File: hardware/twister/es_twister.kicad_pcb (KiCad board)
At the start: 2 copper layers, 22.9 x 38.1 mm, 4 parts, among them J1 T3_Left, J2 T3_Right, J3 T3_Left_B, J4 T3_Right_B

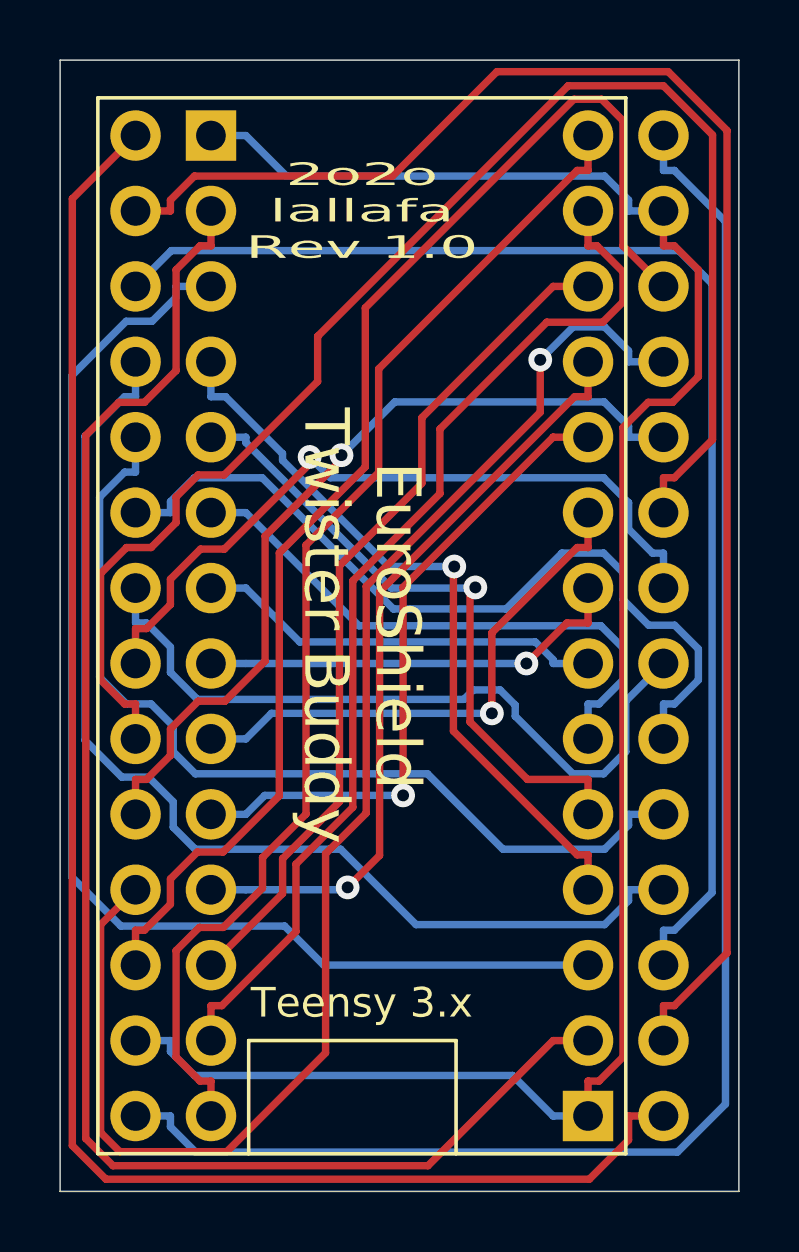
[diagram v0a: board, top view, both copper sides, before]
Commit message: set license: CC-BY-SA-4.0
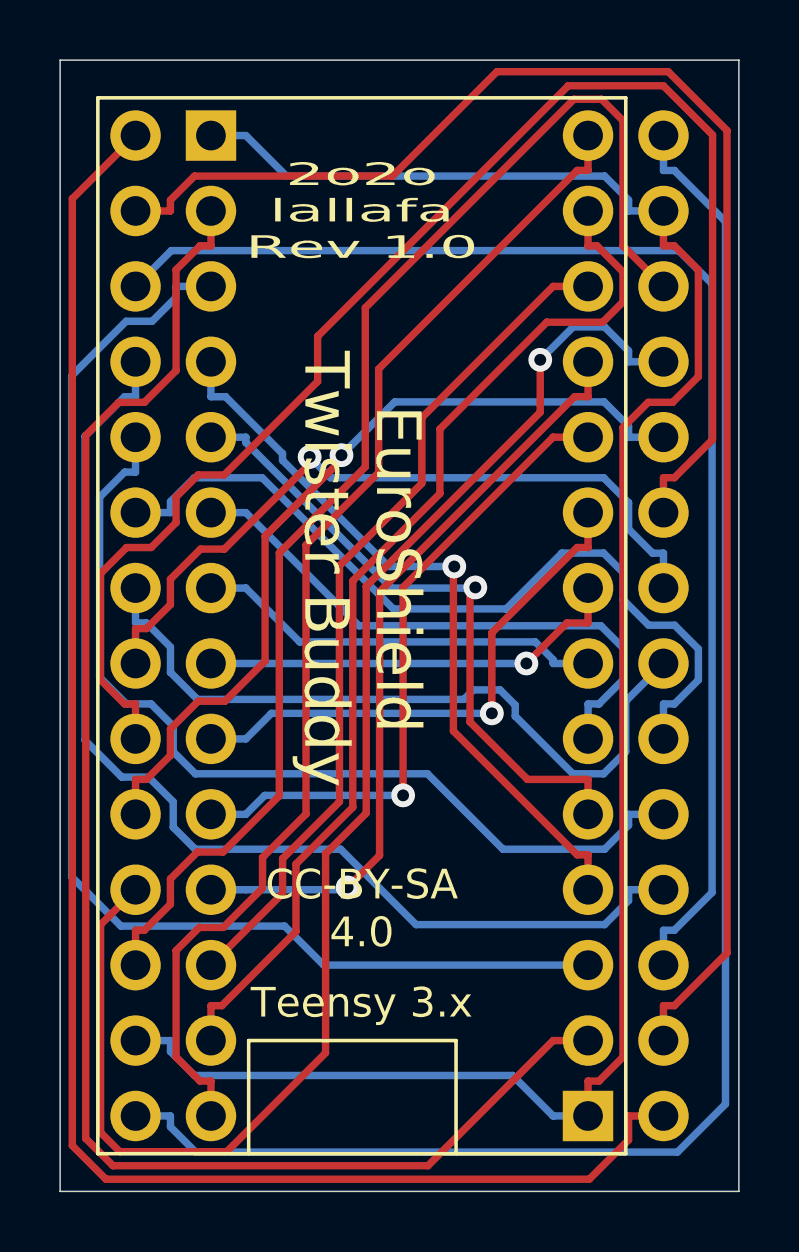
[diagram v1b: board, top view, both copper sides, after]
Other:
- board text added: "CC-BY-SA 4.0"
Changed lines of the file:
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@@
   (general
     (thickness 1.6)
-    (drawings 22)
+    (drawings 23)
     (tracks 330)
     (zones 0)
@@
   (page A4)
   (layers
-    (0 F.Cu signal)
-    (31 B.Cu signal)
+    (0 F.Cu signal hide)
+    (31 B.Cu signal hide)
     (32 B.Adhes user hide)
     (33 F.Adhes user hide)
@@
     )
   )
+  (gr_text "CC-BY-SA\n4.0" (at 142.24 97.155) (layer F.SilkS)
+    (effects (font (size 1 1) (thickness 0.2)))
+  )
   (gr_line (start 135.89 69.85) (end 153.67 69.85) (layer B.SilkS) (width 0.12))
   (gr_line (start 153.67 69.85) (end 153.67 105.41) (layer B.SilkS) (width 0.12))
@@
   )
   (gr_line (start 132.08 106.68) (end 154.94 106.68) (layer Edge.Cuts) (width 0.05))
-  (gr_text "EuroShield\nTwister Buddy" (at 142.24 87.63 270) (layer F.SilkS)
+  (gr_text "EuroShield\nTwister Buddy" (at 142.24 85.725 270) (layer F.SilkS)
     (effects (font (size 1.5 1.5) (thickness 0.3)))
   )
